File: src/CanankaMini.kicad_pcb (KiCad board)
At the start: 2 copper layers, 49.5 x 16.5 mm, 29 parts, among them J1 48037-2200, J2 MC 1,5/4, Q1 DMG2305UX-13, Q2 DMG2305UX-13, U1 MCP2221, U2 PIC18F25K80, U3 MCP2561, U4 AP22652W6-7

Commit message: Removing power-on circuit
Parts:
- removed the C3 at (41.2, 21.5)
- removed the C4 at (49.1, 23.0)
- removed C8: 10u, Medo64:C (0805)
- removed D1: CUS08F30, Medo64:D (SOD323)
- removed DS3: V, Medo64:DS (0805)
- removed the R3 at (50.4, 33.2)
- removed R6: 68K, Medo64:R (0805)
- removed U4: AP22652W6-7, Medo64:U LoadSwitch Adjustable [AP22652W6-7] (SOT23-6)
- DS2: value T -> TERM
- moved R3 13.5 mm to (45.5, 21.6), turned to 0 degrees
- moved R4 12.8 mm to (45.5, 24.0), turned to 0 degrees
- moved R2 10.6 mm to (45.5, 32.5)
- moved DS2 9.88 mm to (50.0, 24.0), turned to 0 degrees
- moved DS1 5.64 mm to (50.0, 32.5), turned to 0 degrees
- moved Q2 3.48 mm to (54.5, 33.7)
- moved Q1 3.48 mm to (54.5, 22.8), turned to 0 degrees
- moved J2 2.55 mm to (59.0, 28.2)
- moved ICON 2.50 mm to (63.5, 28.2)
- moved R1 1.70 mm to (55.5, 28.2), turned to -90 degrees
- renumbered C5 to C3, C6 to C4, C7 to C5, R4 to R3, R5 to R4
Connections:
- J2 pad 4: CAN_V+ -> (no net)
- U2 pad 26: POWER_ON# -> (no net)
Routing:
- net USB_5V: track 32.7 -> 2.66 mm, vias 2 -> 0
- net GND: track 137.2 -> 114.8 mm
- net POWER_ON#: track 15.5 -> 0.00 mm, vias 2 -> 0
- net 5V: track 58.5 -> 73.4 mm, vias 2 -> 5
- net OUT_5V: track 11.5 -> 0.00 mm
- net ILIMIT: track 6.64 -> 0.00 mm
- net CAN_H_SPLIT: track 2.49 -> 8.92 mm, vias 0 -> 2
- net IO_LED_ACTIVITY#: track 3.10 -> 8.60 mm
- net IO_CONTROL_TERMINATE#: track 27.4 -> 31.4 mm, vias 2 -> 3
- net CAN_V+: track 3.60 -> 0.00 mm
- net LED_ACTIVITY: track 9.07 -> 5.78 mm
- net CAN_H: track 12.3 -> 9.24 mm
- net CAN_L_SPLIT: track 2.49 -> 5.32 mm, vias 0 -> 2
- net LED_CAN_TERMINATE: track 7.90 -> 5.30 mm
- net LED_POWER: track 1.95 -> 0.00 mm
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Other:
- board size 49.5 x 16.5 mm -> 47 x 16.5 mm

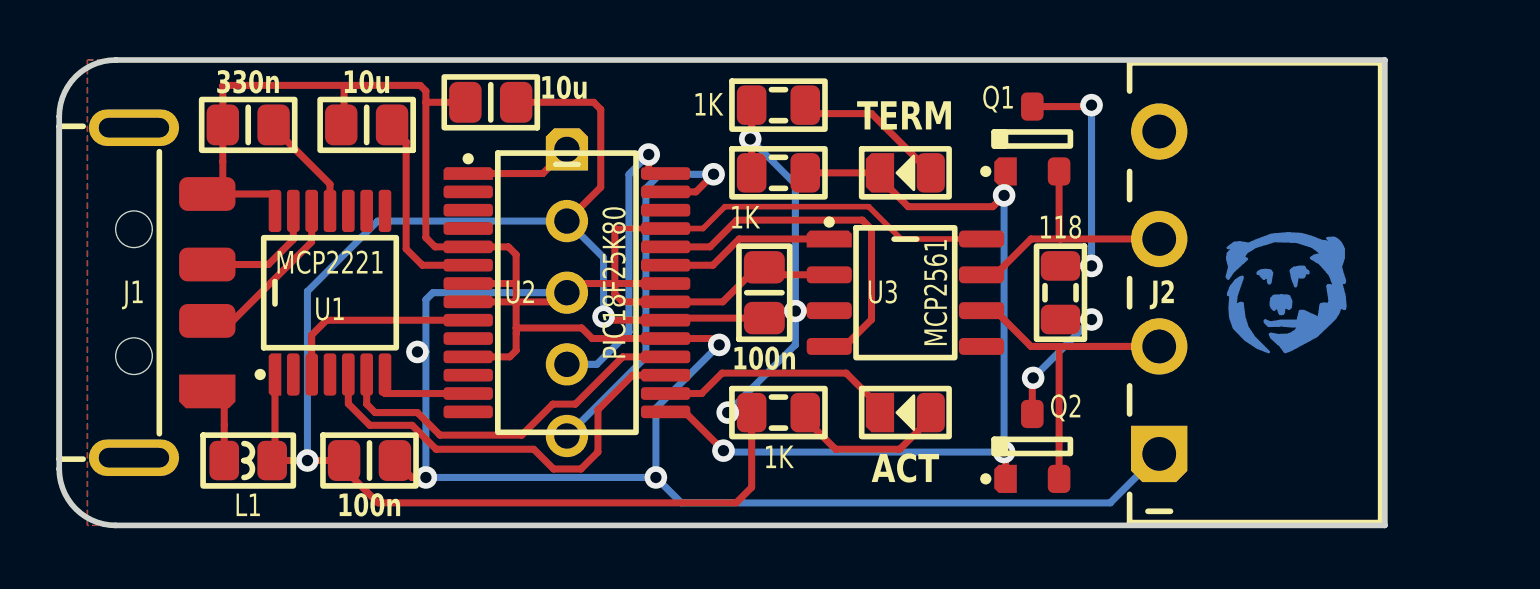
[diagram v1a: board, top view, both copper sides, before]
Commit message: Fixing termination circuit
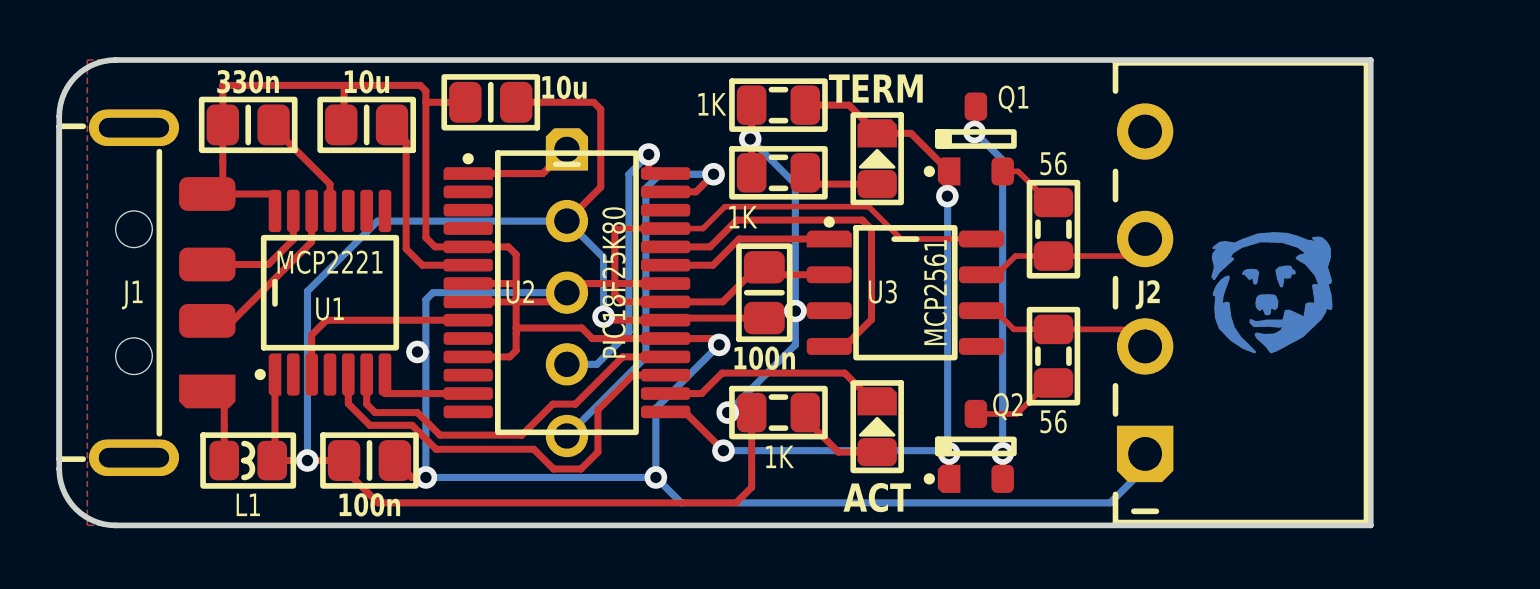
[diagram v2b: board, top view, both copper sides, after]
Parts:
- added R2: 56, Medo64:R (0805), F.Cu at (55.2, 30.5)
- R1: value 118 -> 56
- moved R4 2.40 mm to (45.5, 24.0)
- moved R5 2.40 mm to (45.5, 21.6)
- moved R1 2.26 mm to (55.2, 26.0)
- moved Q1 2.00 mm to (52.5, 22.8)
- moved Q2 2.00 mm to (52.5, 33.7)
- moved DS1 1.12 mm to (49.0, 33.0), turned to -90 degrees
- moved DS2 1.12 mm to (49.0, 23.5), turned to -90 degrees
- moved ICON 0.50 mm to (63.0, 28.2)
- moved J2 0.50 mm to (58.5, 28.2)
- renumbered R2 to R3, R3 to R4, R4 to R5
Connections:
- Q1 pad 2: CAN_H -> CAN_H_TERMINATED
- Q1 pad 3: CAN_H_SPLIT -> CAN_LH_TERMINATED
- Q2 pad 2: CAN_L -> CAN_LH_TERMINATED
- Q2 pad 3: CAN_L_SPLIT -> CAN_L_TERMINATED
- R1 pad 1: CAN_H_SPLIT -> CAN_H_TERMINATED
- R1 pad 2: CAN_L_SPLIT -> CAN_H
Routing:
- net CAN_LH_TERMINATED: track 0.00 -> 13.9 mm, vias 0 -> 2
- net CAN_H_SPLIT: track 8.92 -> 0.00 mm, vias 2 -> 0
- net CAN_L: track 11.5 -> 4.99 mm
- net CAN_L_SPLIT: track 5.32 -> 0.00 mm, vias 2 -> 0
- net IO_CONTROL_TERMINATE#: track 31.4 -> 27.0 mm
- net CAN_H: track 9.24 -> 4.94 mm
- net LED_CAN_TERMINATE: track 5.30 -> 2.15 mm
- net CAN_L_TERMINATED: track 0.00 -> 3.01 mm
- net LED_ACTIVITY: track 5.78 -> 3.04 mm
- net CAN_H_TERMINATED: track 0.00 -> 2.11 mm
- net IO_LED_ACTIVITY#: track 8.60 -> 8.06 mm
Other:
- board size 47 x 16.5 mm -> 46.5 x 16.5 mm

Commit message: Swapped mosfet for a more resilient one
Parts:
- Q1, Q2: value DMG2305UX-13 -> DMP3056L-7
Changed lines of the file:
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@@
 			)
 		)
-		(property "Value" "DMG2305UX-13"
+		(property "Value" "DMP3056L-7"
 			(at 0 2.5 0)
 			(layer "F.SilkS")
@@
 			)
 		)
-		(property "Value" "DMG2305UX-13"
+		(property "Value" "DMP3056L-7"
 			(at 0 2.5 0)
 			(layer "F.SilkS")

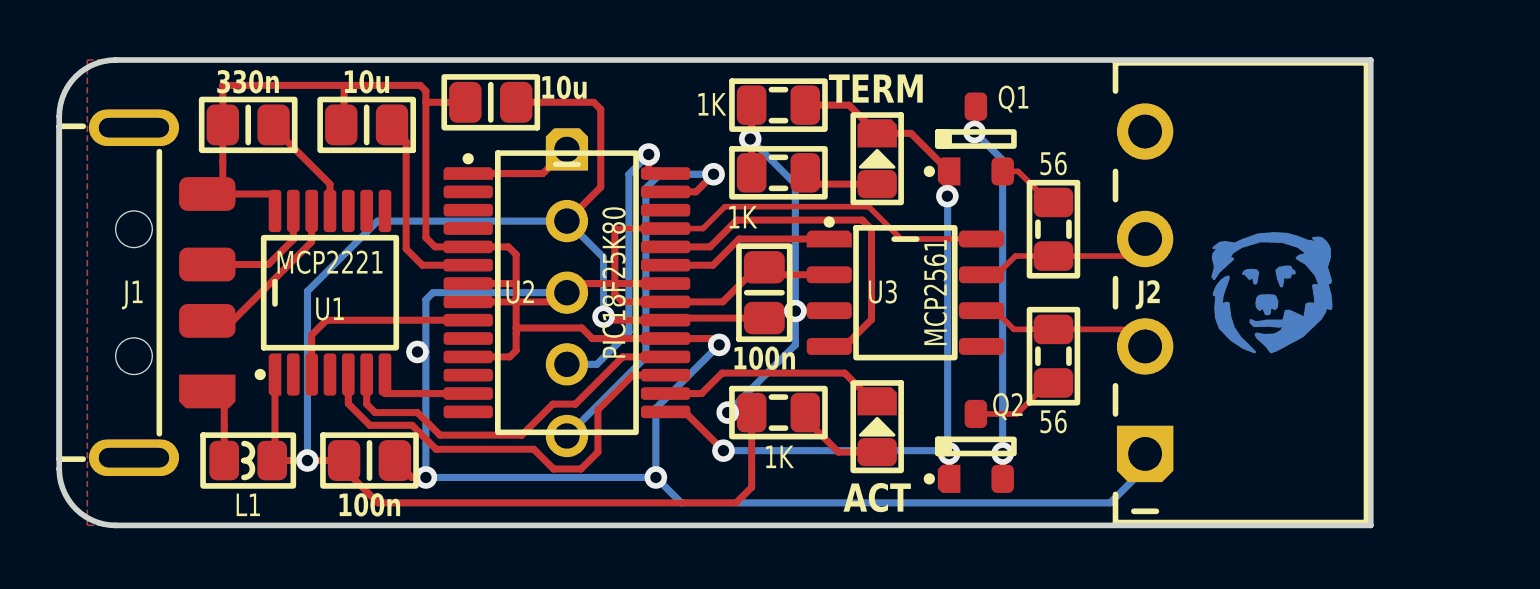
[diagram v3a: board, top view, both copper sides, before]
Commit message: Fixing termination MOSFET connections
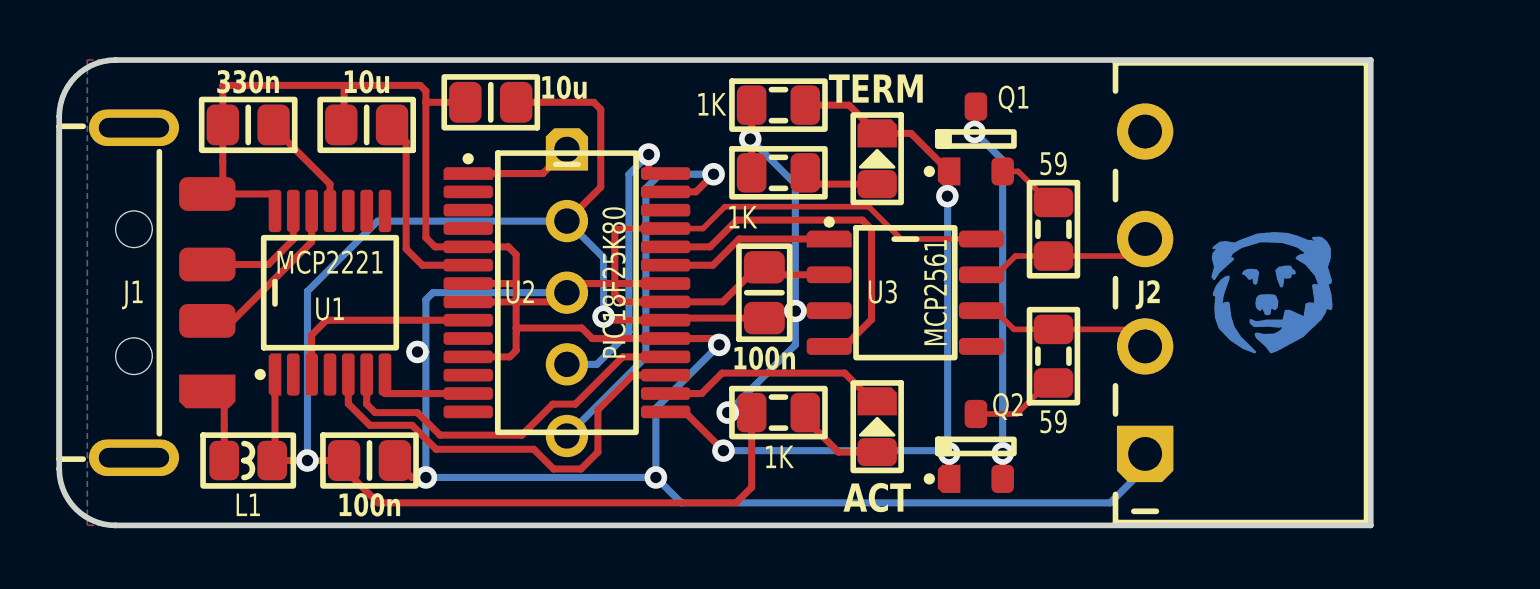
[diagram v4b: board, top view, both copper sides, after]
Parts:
- R1, R2: value 56 -> 59
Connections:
- net CAN_H_TERMINATED renamed CAN_H_TERM
- net CAN_LH_TERMINATED renamed CAN_I_TERM
- net CAN_L_TERMINATED renamed CAN_L_TERM
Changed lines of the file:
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@@
 	(net 21 "LED_CAN_TERMINATE")
 	(net 22 "IO_LED_ACTIVITY#")
-	(net 23 "CAN_L_TERMINATED")
-	(net 24 "CAN_LH_TERMINATED")
-	(net 25 "CAN_H_TERMINATED")
+	(net 23 "CAN_H_TERM")
+	(net 24 "CAN_I_TERM")
+	(net 25 "CAN_L_TERM")
 	(footprint "Medo64:U Micro [PIC18F25K80] (SSOP-28)"
 		(layer "F.Cu")
@@
 			(layers "F.Cu" "F.Paste" "F.Mask")
 			(roundrect_rratio 0.25)
-			(net 25 "CAN_H_TERMINATED")
+			(net 23 "CAN_H_TERM")
 			(thermal_bridge_angle 45)
 		)
@@
 			(layers "F.Cu" "F.Paste" "F.Mask")
 			(roundrect_rratio 0.25)
-			(net 24 "CAN_LH_TERMINATED")
+			(net 24 "CAN_I_TERM")
 			(thermal_bridge_angle 45)
 		)
@@
 			)
 		)
-		(property "Value" "56"
+		(property "Value" "59"
 			(at -2.3 0 0)
 			(layer "F.SilkS")
@@
 			(layers "F.Cu" "F.Paste" "F.Mask")
 			(roundrect_rratio 0.25)
-			(net 25 "CAN_H_TERMINATED")
+			(net 23 "CAN_H_TERM")
 			(thermal_bridge_angle 45)
 		)
@@
 			)
 		)
-		(property "Value" "56"
+		(property "Value" "59"
 			(at -2.35 0 0)
 			(layer "F.SilkS")
@@
 			(layers "F.Cu" "F.Paste" "F.Mask")
 			(roundrect_rratio 0.25)
-			(net 23 "CAN_L_TERMINATED")
+			(net 25 "CAN_L_TERM")
 			(thermal_bridge_angle 45)
 		)
@@
 			(layers "F.Cu" "F.Paste" "F.Mask")
 			(roundrect_rratio 0.25)
-			(net 24 "CAN_LH_TERMINATED")
+			(net 24 "CAN_I_TERM")
 			(thermal_bridge_angle 45)
 		)
@@
 			(layers "F.Cu" "F.Paste" "F.Mask")
 			(roundrect_rratio 0.25)
-			(net 23 "CAN_L_TERMINATED")
+			(net 25 "CAN_L_TERM")
 			(thermal_bridge_angle 45)
 		)
@@
 	)
 	(segment
-		(start 52.5 32.55)
-		(end 53.95 32.55)
+		(start 53.45 23.95)
+		(end 54 23.95)
 		(width 0.2)
 		(layer "F.Cu")
@@
 	)
 	(segment
-		(start 53.95 32.55)
-		(end 55.05 31.45)
+		(start 54 23.95)
+		(end 55.1 25.05)
 		(width 0.2)
 		(layer "F.Cu")
@@
 	)
 	(segment
-		(start 53.45 23.95)
-		(end 54 23.95)
+		(start 52.5 32.55)
+		(end 53.95 32.55)
 		(width 0.2)
 		(layer "F.Cu")
@@
 	)
 	(segment
-		(start 54 23.95)
-		(end 55.1 25.05)
+		(start 53.95 32.55)
+		(end 55.05 31.45)
 		(width 0.2)
 		(layer "F.Cu")
